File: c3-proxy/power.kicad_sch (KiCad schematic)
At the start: 14 parts, among them Q1 DMP2035UQ-7, Q2 DMP2035UQ-7, Q3 DMP2035UQ-7, Q6 31-DMN2053UQ-13CT-ND, SW1 C&K PCM13SMTR, U3 LTC4412xS6, U4 LTC4412xS6

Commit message: final layout and schematic touch ups
killed buzzer
deleted old folder
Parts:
- F2: DIST (none) -> DigiKey; MFR (none) -> Category Circuit Protection, Fuseholders For Use With/Relat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; MPN (none) -> 01550900DR
- Q1, Q2, Q3: DIST (none) -> DigiKey; DPN (none) -> 31-DMP2035UQ-7CT-ND; MFR (none) -> Diodes Incorporated; MPN (none) -> DMP2035UQ-7
- Q6: DIST (none) -> DigiKey; DPN (none) -> 31-DMN2053UQ-13CT-ND; MFR (none) -> Diodes Incorporated; MPN (none) -> DMN2053UQ-13
- R11: DIST (none) -> DigiKey; DPN (none) -> RMCF0603FT10K0CT-ND; MFR (none) -> Stackpole Electronics; MPN (none) -> RMCF0603FT10K0
- R6: footprint oresat-passives:0805-A -> oresat-passives:0603-A; DIST (none) -> DigiKey; DPN (none) -> RMCF0603FT10K0CT-ND; MFR (none) -> Stackpole Electronics; MPN (none) -> RMCF0603FT10K0
- SW1: DIST (none) -> DigiKey; DPN (none) -> 401-2017-1-ND; MFR (none) -> C&K; MPN (none) -> PCM13SMTR
- U3, U4: DIST (none) -> DigiKey; DPN (none) -> LTC4412ES6#WTRMPBF; MFR (none) -> Analog Devices; MPN (none) -> LTC4412ES6#PBF
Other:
- note added: "Reversed PMOS for ideal diode"

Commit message: Fix library paths and start fixing ERCs
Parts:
- TP18, TP19, TP20, TP21: symbol oresat_stuff:Test-Point-0.75mm-th -> oresat-misc:Test-Point-0.75mm-th
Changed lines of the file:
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@@
 	)
 	(symbol
-		(lib_id "oresat_stuff:Test-Point-0.75mm-th")
+		(lib_id "oresat-misc:Test-Point-0.75mm-th")
 		(at 199.39 158.75 0)
 		(mirror y)
@@
 	)
 	(symbol
-		(lib_id "oresat_stuff:VBUS")
+		(lib_id "power:VBUS")
 		(at 165.1 185.42 0)
 		(mirror y)
@@
 	)
 	(symbol
-		(lib_id "oresat_stuff:VBUS")
+		(lib_id "power:VBUS")
 		(at 180.34 130.81 0)
 		(unit 1)
@@
 	)
 	(symbol
-		(lib_id "oresat_stuff:VBUS")
+		(lib_id "power:VBUS")
 		(at 241.3 67.31 0)
 		(unit 1)
@@
 	)
 	(symbol
-		(lib_id "oresat_stuff:Test-Point-0.75mm-th")
+		(lib_id "oresat-misc:Test-Point-0.75mm-th")
 		(at 198.12 213.36 0)
 		(mirror y)
@@
 	)
 	(symbol
-		(lib_id "oresat_stuff:Test-Point-0.75mm-th")
+		(lib_id "oresat-misc:Test-Point-0.75mm-th")
 		(at 224.79 158.75 0)
 		(unit 1)
@@
 	)
 	(symbol
-		(lib_id "oresat_stuff:Test-Point-0.75mm-th")
+		(lib_id "oresat-misc:Test-Point-0.75mm-th")
 		(at 226.06 213.36 0)
 		(unit 1)

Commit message: did like... everything...
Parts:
- removed TP18, TP19, TP20, TP21: Test-Point, oresat-misc:TestPoint-0.75mm-th, symbol oresat-misc:Test-Point-0.75mm-th
- added D6: 1N4001, Diode_THT:D_DO-35_SOD27_P7.62mm_Horizontal, symbol Diode:1N4151
- added F1: 0451004.MRL (4A), symbol Device:Fuse
- F2: DPN (none) -> 18-01550900DRTR-ND
- SW1: footprint oresat-misc:SW-CK-PCM13SMTR -> SWITCH_3SMTR; symbol oresat_stuff:C&K PCM13SMTR -> oresat-misc:C&K PCM13SMTR
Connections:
- net GND: now also D6.2 (A)
- net at F2.1, Q2.1 (D), U4.1 (VIN): now also D6.1 (K)
- no-connect marks 1 -> 7
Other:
- note added: "fuse holder"
- note added: "reverse polarity protection. CERTIFIED: undergraduate proof!!!"
- note removed: "3A fuse"
- moved on the sheet: F2

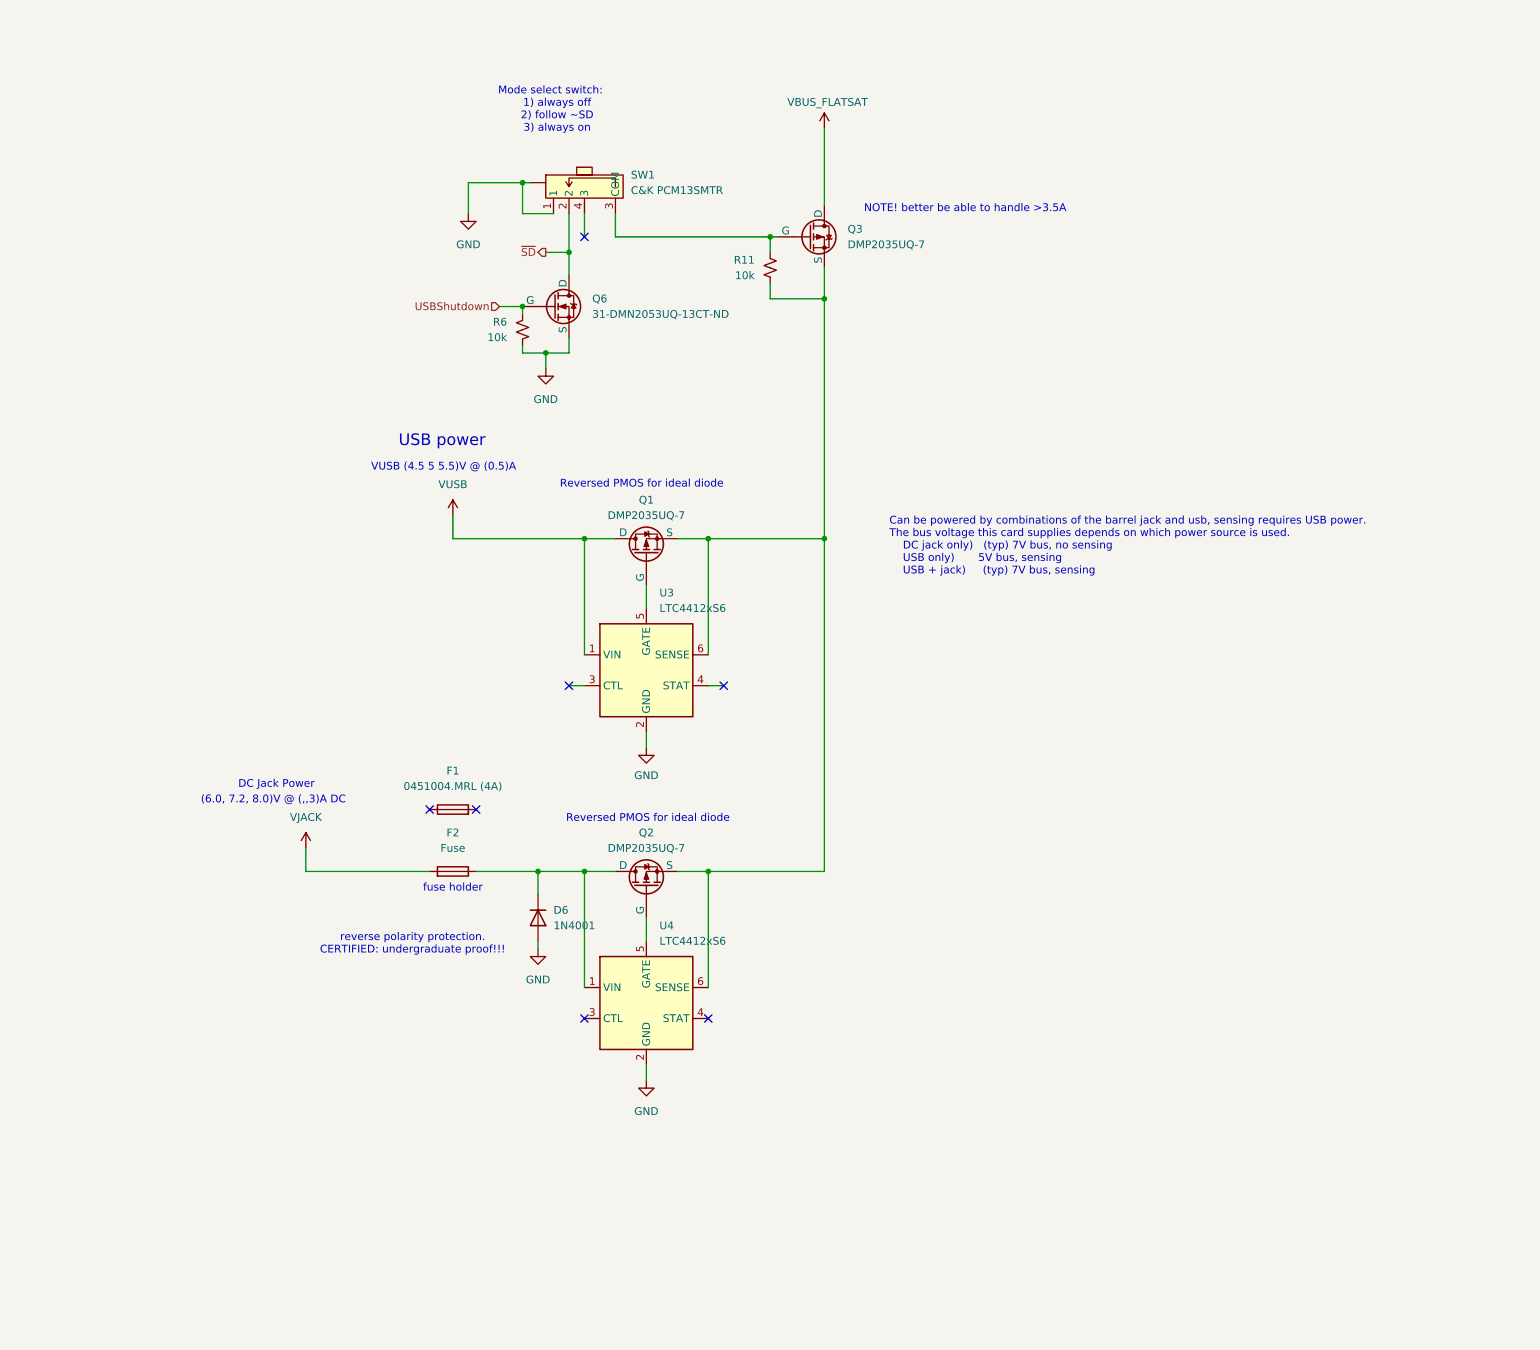
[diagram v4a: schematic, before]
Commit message: v1.0 of the C3 Proxy sent off to fabrication.
Added makefile and README. Fixed a bunch of BOM issues, mostly just EOL and out of stock components. Fixed wrong footprints in the BOM, and switched diode from TH to SMT. Cleaned up some traces for funsies,
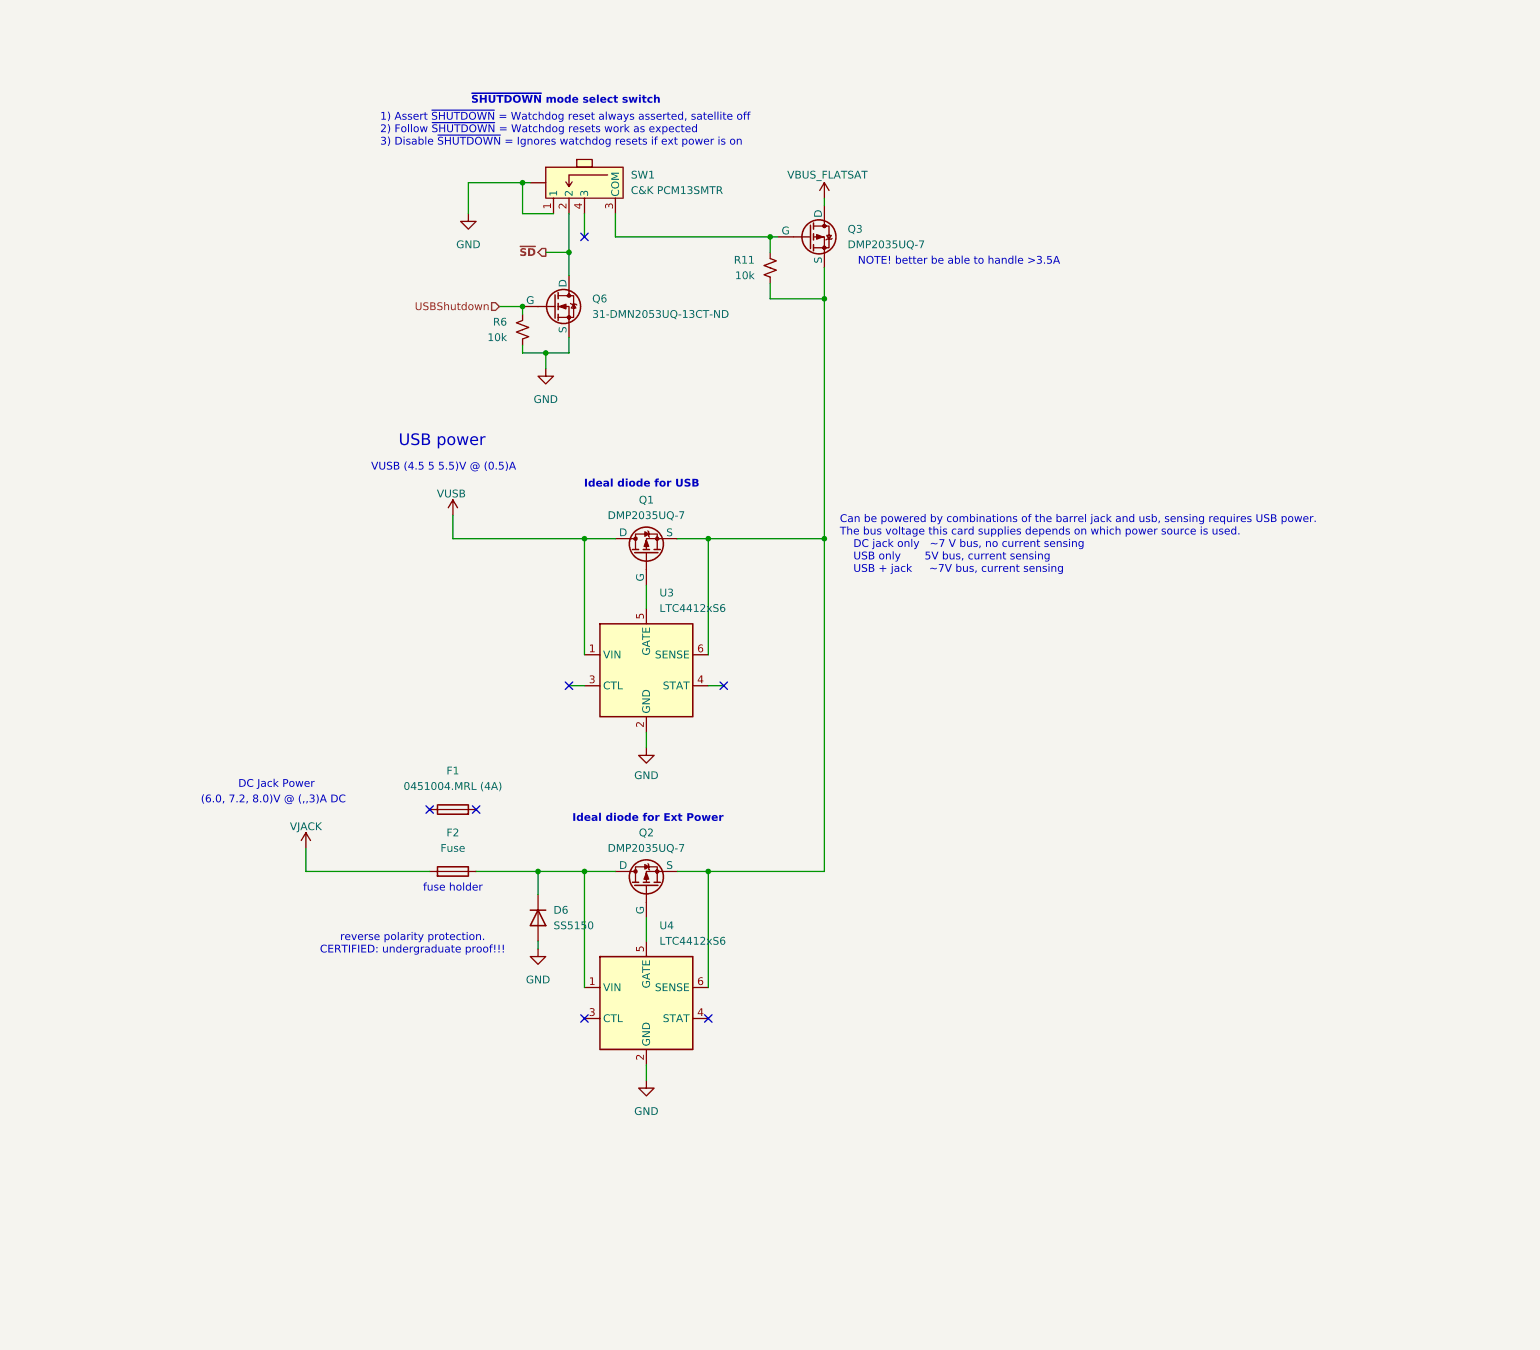
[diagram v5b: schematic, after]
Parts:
- D6: value 1N4001 -> SS5150; footprint Diode_THT:D_DO-35_SOD27_P7.62mm_Horizontal -> Diode_SMD:D_SMA; DPN 4878-1N4001CT-ND -> 5399-SS5150CT-ND; MFR Diotec Semiconductor -> Shenzhen Slkormicro Semicon Co., Ltd.; MPN 1N4001 -> SS5150
- F1: DPN F2586TR-ND -> F2586CT-ND
- F2: DPN 18-01550900DRTR-ND -> 18-01550900DRCT-ND
- SW1: footprint SWITCH_3SMTR -> oresat-misc:SW-CK-PCM13SMTR
- U3, U4: DPN LTC4412ES6#WTRMPBF -> 505-LTC4412ES6#WTRMPBFCT-ND; MPN LTC4412ES6#PBF -> LTC4412ES6#WTRMPBF
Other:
- note added: "1) Assert ~{SHUTDOWN} = Watchdog reset always asserted, satellite off 2) Follow ~{SHUTDOWN} = Watchdog resets work as expected 3) Disable ~{SHUTDOWN} = Ignores watchdog resets if ext power is on"
- note added: "Can be powered by combinations of the barrel jack and usb, sensing requires USB power. The bus voltage this card supplies depends on which power source is used. DC jack only ~7 V bus, no current sensing USB only 5V bus, current sensing USB + jack ~7V bus, current sensing"
- note added: "Ideal diode for Ext Power"
- note added: "Ideal diode for USB"
- note added: "~{SHUTDOWN} mode select switch"
- note removed: "Can be powered by combinations of the barrel jack and usb, sensing requires USB power. The bus voltage this card supplies depends on which power source is used. DC jack only) (typ) 7V bus, no sensing USB only) 5V bus, sensing USB + jack) (typ) 7V bus, sensing"
- note removed: "Mode select switch: 1) always off 2) follow ~SD 3) always on"
- note removed: "Reversed PMOS for ideal diode"
- moved on the sheet: SW1
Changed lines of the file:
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@@
+		)
+	)
+	(text "~{SHUTDOWN} mode select switch"
+		(exclude_from_sim no)
+		(at 198.882 62.738 0)
+		(effects
+			(font
+				(size 1.27 1.27)
+				(thickness 0.254)
+				(bold yes)
+			)
 		)
 	)
@@
 		)
 	)
-	(text "Can be powered by combinations of the barrel jack and usb, sensing requires USB power.\nThe bus voltage this card supplies depends on which power source is used.\n	DC jack only)   (typ) 7V bus, no sensing\n	USB only)       5V bus, sensing\n	USB + jack)     (typ) 7V bus, sensing"
+	(text "Can be powered by combinations of the barrel jack and usb, sensing requires USB power.\nThe bus voltage this card supplies depends on which power source is used.\n	DC jack only   ~7 V bus, no current sensing\n	USB only       5V bus, current sensing\n	USB + jack     ~7V bus, current sensing"
 		(exclude_from_sim no)
-		(at 251.968 135.89 0)
+		(at 243.84 135.636 0)
 		(effects
 			(font
@@
 		)
 	)
-	(text "Reversed PMOS for ideal diode"
+	(text "Ideal diode for USB"
 		(exclude_from_sim no)
 		(at 211.328 125.73 0)
@@
 			(font
 				(size 1.27 1.27)
+				(thickness 0.254)
+				(bold yes)
 			)
 		)
@@
 		)
 	)
-	(text "Mode select switch:\n	1) always off\n	2) follow ~SD\n	3) always on"
+	(text "1) Assert ~{SHUTDOWN} = Watchdog reset always asserted, satellite off\n2) Follow ~{SHUTDOWN} = Watchdog resets work as expected\n3) Disable ~{SHUTDOWN} = Ignores watchdog resets if ext power is on"
 		(exclude_from_sim no)
-		(at 196.342 64.262 0)
+		(at 168.402 67.564 0)
 		(effects
 			(font
 				(size 1.27 1.27)
 			)
-		)
-	)
-	(text "Reversed PMOS for ideal diode"
+			(justify left)
+		)
+	)
+	(text "Ideal diode for Ext Power\n"
 		(exclude_from_sim no)
 		(at 212.344 180.594 0)
@@
 			(font
 				(size 1.27 1.27)
+				(thickness 0.254)
+				(bold yes)
 			)
 		)
@@
 	(text "NOTE! better be able to handle >3.5A\n"
 		(exclude_from_sim no)
-		(at 264.414 80.518 0)
+		(at 263.398 89.154 0)
 		(effects
 			(font
@@
 	(wire
 		(pts
-			(xy 241.3 67.31) (xy 241.3 80.01)
+			(xy 241.3 78.74) (xy 241.3 80.01)
 		)
 		(stroke
@@
 			(font
 				(size 1.27 1.27)
+				(thickness 0.254)
+				(bold yes)
 			)
 			(justify right)
@@
 			)
 		)
-		(property "DPN" "F2586TR-ND"
+		(property "DPN" "F2586CT-ND"
 			(at 180.34 179.07 90)
 			(hide yes)
@@
 			)
 		)
-		(property "Value" "1N4001"
+		(property "Value" "SS5150"
 			(at 196.85 198.1199 90)
 			(show_name no)
@@
 			)
 		)
-		(property "Footprint" "Diode_THT:D_DO-35_SOD27_P7.62mm_Horizontal"
+		(property "Footprint" "Diode_SMD:D_SMA"
 			(at 189.865 196.85 0)
 			(hide yes)
@@
 			)
 		)
-		(property "Description" "Diode 50 V 1A Through Hole DO-204AC (DO-41)"
+		(property "Description" "Diode 150 V 5A Surface Mount DO-214AC (SMA)"
 			(at 194.31 196.85 0)
 			(hide yes)
@@
 			)
 		)
-		(property "DPN" "4878-1N4001CT-ND"
+		(property "DPN" "5399-SS5150CT-ND"
 			(at 194.31 196.85 90)
 			(hide yes)
@@
 			)
 		)
-		(property "MFR" "Diotec Semiconductor"
+		(property "MFR" "Shenzhen Slkormicro Semicon Co., Ltd."
 			(at 194.31 196.85 90)
 			(hide yes)
@@
 			)
 		)
-		(property "MPN" "1N4001"
+		(property "MPN" "SS5150"
 			(at 194.31 196.85 90)
 			(hide yes)
@@
 			)
 		)
-		(property "DPN" "18-01550900DRTR-ND"
+		(property "DPN" "18-01550900DRCT-ND"
 			(at 180.34 189.23 90)
 			(hide yes)
@@
 		(in_pos_files yes)
 		(dnp no)
-		(fields_autoplaced yes)
 		(property "Reference" "#VBUS015"
 			(at 156.21 189.23 0)
@@
 		)
 		(property "Value" "VJACK"
-			(at 156.21 180.34 0)
+			(at 156.21 181.864 0)
 			(show_name no)
 			(do_not_autoplace no)
@@
 		(in_pos_files yes)
 		(dnp no)
-		(fields_autoplaced yes)
 		(property "Reference" "#VBUS03"
 			(at 180.34 134.62 0)
@@
 		)
 		(property "Value" "VUSB"
-			(at 180.34 125.73 0)
+			(at 180.086 127.254 0)
 			(show_name no)
 			(do_not_autoplace no)
@@
 	(symbol
 		(lib_id "power:VBUS")
-		(at 241.3 67.31 0)
+		(at 241.3 78.74 0)
 		(unit 1)
 		(body_style 1)
@@
 		(dnp no)
 		(property "Reference" "#VBUS010"
-			(at 241.3 71.12 0)
+			(at 241.3 82.55 0)
 			(hide yes)
 			(show_name no)
@@
 		)
 		(property "Value" "VBUS_FLATSAT"
-			(at 235.204 62.992 0)
+			(at 235.204 74.93 0)
 			(show_name no)
 			(do_not_autoplace no)
@@
 		)
 		(property "Footprint" ""
-			(at 241.3 67.31 0)
+			(at 241.3 78.74 0)
 			(hide yes)
 			(show_name no)
@@
 		)
 		(property "Datasheet" ""
-			(at 241.3 67.31 0)
+			(at 241.3 78.74 0)
 			(hide yes)
 			(show_name no)
@@
 		)
 		(property "Description" "Power symbol creates a global label with name \"VBUS\""
-			(at 241.3 67.31 0)
+			(at 241.3 78.74 0)
 			(hide yes)
 			(show_name no)
@@
 			)
 		)
-		(property "DPN" "LTC4412ES6#WTRMPBF"
+		(property "DPN" "505-LTC4412ES6#WTRMPBFCT-ND"
 			(at 212.09 210.82 0)
 			(hide yes)
@@
 			)
 		)
-		(property "MPN" "LTC4412ES6#PBF"
+		(property "MPN" "LTC4412ES6#WTRMPBF"
 			(at 212.09 210.82 0)
 			(hide yes)
@@
 			)
 		)
-		(property "Footprint" "SWITCH_3SMTR"
+		(property "Footprint" "oresat-misc:SW-CK-PCM13SMTR"
 			(at 201.93 58.166 0)
 			(hide yes)
@@
 			)
 		)
-		(property "DPN" "LTC4412ES6#WTRMPBF"
+		(property "DPN" "505-LTC4412ES6#WTRMPBFCT-ND"
 			(at 212.09 156.21 0)
 			(hide yes)
@@
 			)
 		)
-		(property "MPN" "LTC4412ES6#PBF"
+		(property "MPN" "LTC4412ES6#WTRMPBF"
 			(at 212.09 156.21 0)
 			(hide yes)

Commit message: decreased size to fit in EU, transistor orientation
changed DC jack to be edge connected.
adjusted layout in top-right corner to still fit mounting hole.
fixed transistor orientation by switching to GSD symbols
moved SW2 and clarified silkscreen with boxes
changed via sizes to be standardized
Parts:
- removed Q1, Q2, Q3: DMP2035UQ-7, Package_TO_SOT_SMD:SOT-23-3, symbol Simulation_SPICE:PMOS
- removed Q6: 31-DMN2053UQ-13CT-ND, Package_TO_SOT_SMD:SOT-23-3, symbol Simulation_SPICE:NMOS
- added Q2, Q5, Q7: DMP2035UQ-7, Package_TO_SOT_SMD:SOT-23-3, symbol Transistor_FET:Q_PMOS_GSD
- added Q6: 31-DMN2053UQ-13CT-ND, Package_TO_SOT_SMD:SOT-23-3, symbol Transistor_FET_Other:Q_NMOS_Depletion_GSD
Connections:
- net GND: now also Q6.2 (S)
- net USBShutdown: now also Q6.1 (G)
- net VBUS_FLATSAT: now also Q7.3 (D)
- net VUSB: now also Q5.3 (D)
- net ~{SD}: now also Q6.3 (D)
- net at D6.1 (K), F2.1, U4.1 (VIN): now also Q2.3 (D)
- net at U3.5 (GATE): now also Q5.1 (G)
- net at R11.2, U3.6 (SENSE), U4.6 (SENSE): now also Q2.2 (S), Q5.2 (S), Q7.2 (S)
- net at R11.1, SW1.3 (COM): now also Q7.1 (G)
- net at U4.5 (GATE): now also Q2.1 (G)
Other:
- title: Flatsat Interface Card -> c3-Proxy card

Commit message: changed footprints in schematic
so that "update from schematic" doesn't kill my baby resistors
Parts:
- R11, R6: footprint oresat-passives:0603-A -> oresat-passives:0603-C-NOSILK
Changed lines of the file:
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@@
 			)
 		)
-		(property "Footprint" "oresat-passives:0603-A"
+		(property "Footprint" "oresat-passives:0603-C-NOSILK"
 			(at 232.41 90.17 0)
 			(hide yes)
@@
 			)
 		)
-		(property "Footprint" "oresat-passives:0603-A"
+		(property "Footprint" "oresat-passives:0603-C-NOSILK"
 			(at 191.77 100.33 0)
 			(hide yes)
